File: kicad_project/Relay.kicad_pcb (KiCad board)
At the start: 2 copper layers, 36.6 x 28.3 mm, 13 parts, among them J1 5018762640, J2 USB_C_Receptacle, J3 RJ45, K1 G6K-2P-Y_DC5, Q1 CMPT5551

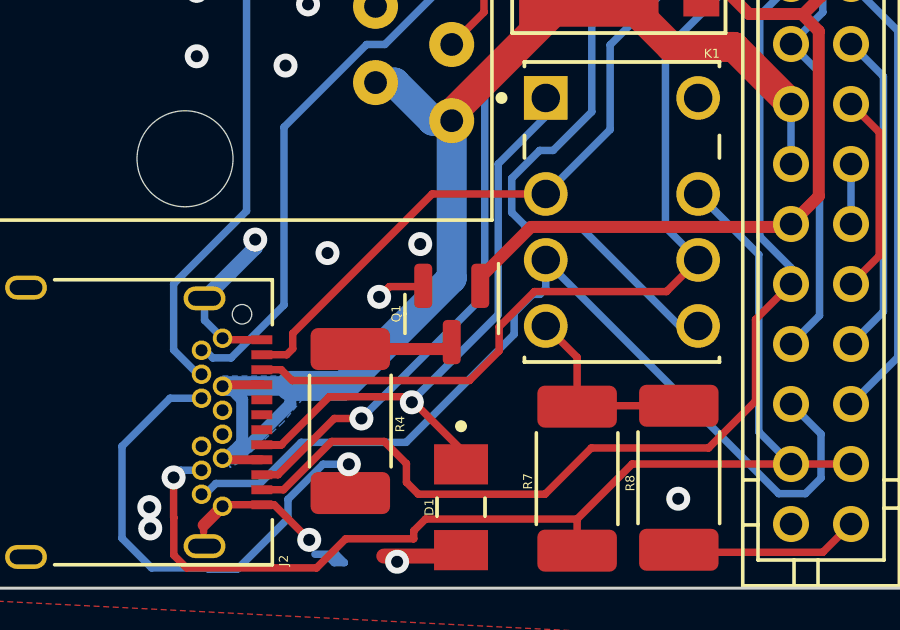
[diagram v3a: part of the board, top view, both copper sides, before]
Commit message: finally fixed Transistor Issue. credits to mlocoteta
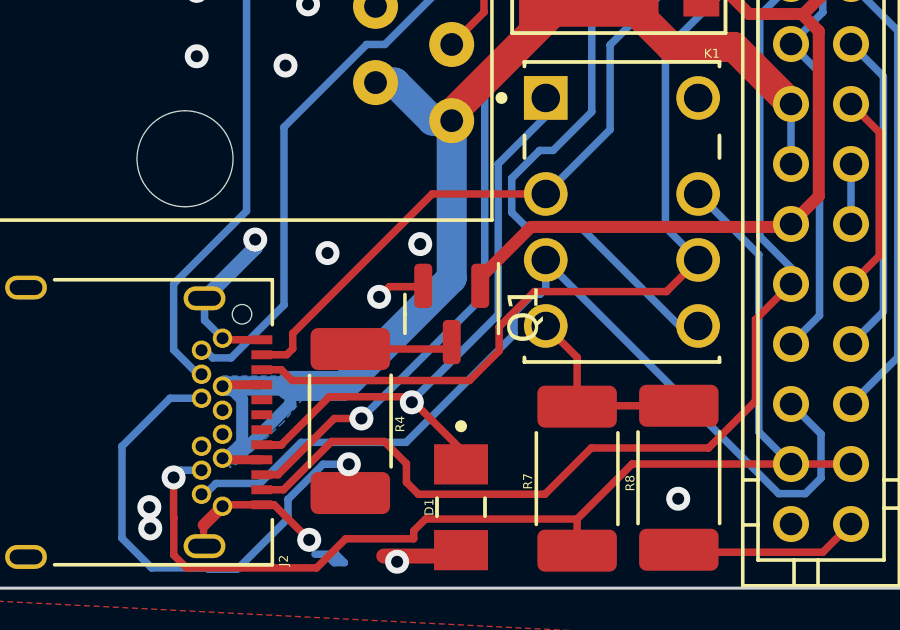
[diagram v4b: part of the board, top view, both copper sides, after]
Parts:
- Q1: value CMPT5551 -> DDTC114ECA-7-F
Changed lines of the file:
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@@
   (net 28 "CAN2_H")
   (net 29 "Relay_5")
-  (net 30 "Net-(Q1-Pad3)")
-  (footprint "Package_TO_SOT_SMD:SOT-23" (layer "F.Cu")
-    (at 162.84 71.59 -90)
-    (descr "SOT, 3 Pin (https://www.jedec.org/system/files/docs/to-236h.pdf variant AB), generated with kicad-footprint-generator ipc_gullwing_generator.py")
-    (tags "SOT TO_SOT_SMD")
-    (property "Sheetfile" "Relay.kicad_sch")
-    (property "Sheetname" "")
-    (attr smd)
-    (fp_text reference "Q1" (at -0.01 1.85 -90) (layer "F.SilkS")
-      (effects (font (size 0.3 0.3) (thickness 0.15)))
-    )
-    (fp_text value "CMPT5551" (at 0 2.4 90) (layer "F.Fab")
-      (effects (font (size 1 1) (thickness 0.15)))
-    )
-    (fp_text user "${REFERENCE}" (at 0 0 90) (layer "F.Fab")
-      (effects (font (size 0.32 0.32) (thickness 0.05)))
-    )
-    (fp_line (start 0 1.56) (end -0.65 1.56) (layer "F.SilkS") (width 0.12))
-    (fp_line (start 0 -1.56) (end -1.675 -1.56) (layer "F.SilkS") (width 0.12))
-    (fp_line (start 0 -1.56) (end 0.65 -1.56) (layer "F.SilkS") (width 0.12))
-    (fp_line (start 0 1.56) (end 0.65 1.56) (layer "F.SilkS") (width 0.12))
-    (fp_line (start 1.92 -1.7) (end -1.92 -1.7) (layer "F.CrtYd") (width 0.05))
-    (fp_line (start -1.92 -1.7) (end -1.92 1.7) (layer "F.CrtYd") (width 0.05))
-    (fp_line (start -1.92 1.7) (end 1.92 1.7) (layer "F.CrtYd") (width 0.05))
-    (fp_line (start 1.92 1.7) (end 1.92 -1.7) (layer "F.CrtYd") (width 0.05))
-    (fp_line (start -0.65 -1.125) (end -0.325 -1.45) (layer "F.Fab") (width 0.1))
-    (fp_line (start 0.65 -1.45) (end 0.65 1.45) (layer "F.Fab") (width 0.1))
-    (fp_line (start 0.65 1.45) (end -0.65 1.45) (layer "F.Fab") (width 0.1))
-    (fp_line (start -0.325 -1.45) (end 0.65 -1.45) (layer "F.Fab") (width 0.1))
-    (fp_line (start -0.65 1.45) (end -0.65 -1.125) (layer "F.Fab") (width 0.1))
-    (pad "1" smd roundrect (at -0.9375 -0.95 270) (size 1.475 0.6) (layers "F.Cu" "F.Paste" "F.Mask") (roundrect_rratio 0.25)
-      (net 3 "IGN") (pinfunction "B") (pintype "input"))
-    (pad "2" smd roundrect (at -0.9375 0.95 270) (size 1.475 0.6) (layers "F.Cu" "F.Paste" "F.Mask") (roundrect_rratio 0.25)
-      (net 2 "GND") (pinfunction "E") (pintype "passive"))
-    (pad "3" smd roundrect (at 0.9375 0 270) (size 1.475 0.6) (layers "F.Cu" "F.Paste" "F.Mask") (roundrect_rratio 0.25)
-      (net 30 "Net-(Q1-Pad3)") (pinfunction "C") (pintype "passive"))
-    (model "${KICAD6_3DMODEL_DIR}/Package_TO_SOT_SMD.3dshapes/SOT-23.wrl"
-      (offset (xyz 0 0 0))
-      (scale (xyz 1 1 1))
-      (rotate (xyz 0 0 0))
-    )
-  )
+  (net 30 "Net-(R4-Pad1)")
   (footprint "Relay:DIO_BAV21W_RHG" (layer "F.Cu")
     (at 163.15 78.0325 -90)
@@
     )
   )
+  (footprint "Package_TO_SOT_SMD:SOT-23" (layer "F.Cu")
+    (at 162.84 71.59 -90)
+    (descr "SOT, 3 Pin (https://www.jedec.org/system/files/docs/to-236h.pdf variant AB), generated with kicad-footprint-generator ipc_gullwing_generator.py")
+    (tags "SOT TO_SOT_SMD")
+    (property "Sheetfile" "Relay.kicad_sch")
+    (property "Sheetname" "")
+    (attr smd)
+    (fp_text reference "Q1" (at 0 -2.4 90) (layer "F.SilkS")
+      (effects (font (size 1 1) (thickness 0.15)))
+    )
+    (fp_text value "DDTC114ECA-7-F " (at 0 2.4 90) (layer "F.Fab")
+      (effects (font (size 1 1) (thickness 0.15)))
+    )
+    (fp_text user "${REFERENCE}" (at 0 0 90) (layer "F.Fab")
+      (effects (font (size 0.32 0.32) (thickness 0.05)))
+    )
+    (fp_line (start 0 1.56) (end 0.65 1.56) (layer "F.SilkS") (width 0.12))
+    (fp_line (start 0 -1.56) (end 0.65 -1.56) (layer "F.SilkS") (width 0.12))
+    (fp_line (start 0 1.56) (end -0.65 1.56) (layer "F.SilkS") (width 0.12))
+    (fp_line (start 0 -1.56) (end -1.675 -1.56) (layer "F.SilkS") (width 0.12))
+    (fp_line (start 1.92 1.7) (end 1.92 -1.7) (layer "F.CrtYd") (width 0.05))
+    (fp_line (start -1.92 -1.7) (end -1.92 1.7) (layer "F.CrtYd") (width 0.05))
+    (fp_line (start 1.92 -1.7) (end -1.92 -1.7) (layer "F.CrtYd") (width 0.05))
+    (fp_line (start -1.92 1.7) (end 1.92 1.7) (layer "F.CrtYd") (width 0.05))
+    (fp_line (start 0.65 -1.45) (end 0.65 1.45) (layer "F.Fab") (width 0.1))
+    (fp_line (start -0.65 -1.125) (end -0.325 -1.45) (layer "F.Fab") (width 0.1))
+    (fp_line (start -0.65 1.45) (end -0.65 -1.125) (layer "F.Fab") (width 0.1))
+    (fp_line (start 0.65 1.45) (end -0.65 1.45) (layer "F.Fab") (width 0.1))
+    (fp_line (start -0.325 -1.45) (end 0.65 -1.45) (layer "F.Fab") (width 0.1))
+    (pad "1" smd roundrect (at -0.9375 -0.95 270) (size 1.475 0.6) (layers "F.Cu" "F.Paste" "F.Mask") (roundrect_rratio 0.25)
+      (net 3 "IGN") (pinfunction "B") (pintype "input"))
+    (pad "2" smd roundrect (at -0.9375 0.95 270) (size 1.475 0.6) (layers "F.Cu" "F.Paste" "F.Mask") (roundrect_rratio 0.25)
+      (net 2 "GND") (pinfunction "E") (pintype "passive"))
+    (pad "3" smd roundrect (at 0.9375 0 270) (size 1.475 0.6) (layers "F.Cu" "F.Paste" "F.Mask") (roundrect_rratio 0.25)
+      (net 30 "Net-(R4-Pad1)") (pinfunction "C") (pintype "passive"))
+    (model "${KICAD6_3DMODEL_DIR}/Package_TO_SOT_SMD.3dshapes/SOT-23.wrl"
+      (offset (xyz 0 0 0))
+      (scale (xyz 1 1 1))
+      (rotate (xyz 0 0 0))
+    )
+  )
   (footprint "Resistor_SMD:R_0603_1608Metric" (layer "F.Cu")
     (at 166.15 56.71 180)
@@
     (fp_line (start -2.5 1.25) (end -2.5 -1.25) (layer "F.Fab") (width 0.1))
     (pad "1" smd roundrect (at -2.4 0 270) (size 1.4 2.65) (layers "F.Cu" "F.Paste" "F.Mask") (roundrect_rratio 0.1785707143)
-      (net 30 "Net-(Q1-Pad3)") (pintype "passive"))
+      (net 30 "Net-(R4-Pad1)") (pintype "passive"))
     (pad "2" smd roundrect (at 2.4 0 270) (size 1.4 2.65) (layers "F.Cu" "F.Paste" "F.Mask") (roundrect_rratio 0.1785707143)
       (net 21 "SBU2") (pintype "passive"))
@@
   (segment (start 167.5086 64.8514) (end 166.22 66.14) (width 0.25) (layer "B.Cu") (net 29))
   (segment (start 170.43 71.99) (end 171.0545 71.99) (width 0.25) (layer "B.Cu") (net 29))
-  (segment (start 159.46 72.76) (end 162.6075 72.76) (width 0.4) (layer "F.Cu") (net 30))
   (segment (start 162.6075 72.76) (end 162.84 72.5275) (width 0.25) (layer "F.Cu") (net 30))
+  (segment (start 159.46 72.76) (end 162.6075 72.76) (width 0.25) (layer "F.Cu") (net 30))
   (zone (net 2) (net_name "GND") (layer "F.Cu") (hatch edge 0.508)
     (connect_pads (clearance 0.508))

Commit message: tested
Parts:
- moved R5 5.46 mm to (170.6, 53.5)
- moved D1 4.78 mm to (160.1, 74.4), turned to 90 degrees
- moved R6 3.92 mm to (166.8, 53.5)
- moved R4 3.87 mm to (163.0, 76.7)
- moved R1 1.84 mm to (168.7, 55.9)
- moved Q1 0.68 mm to (163.1, 71.0)
- turned CR1 to 180 degrees
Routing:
- net GND: track 16.5 -> 59.1 mm, vias 18 -> 12
- net CAN1_L: track 54.3 -> 30.7 mm, vias 1 -> 0
- net CAN0_L: track 38.2 -> 50.0 mm, vias 0 -> 3
- net CAN0_H: track 32.4 -> 41.8 mm, vias 0 -> 2
- net Net-(J3-Pad3): track 6.29 -> 13.2 mm
- net +12V: track 45.3 -> 39.6 mm
- net Relay_5: track 25.8 -> 20.1 mm
- net CAN3_H: track 17.5 -> 22.0 mm
- net Net-(J1-Pad5): track 13.5 -> 17.6 mm
- net CAN2_L: track 39.5 -> 42.7 mm
- net CAN3_L: track 22.4 -> 25.2 mm
- net IGN: track 37.5 -> 39.4 mm, vias 0 -> 2
- net CAN2_H: track 31.2 -> 32.5 mm
- net Net-(J1-Pad21): track 15.3 -> 16.5 mm
- net SBU1: track 21.2 -> 20.0 mm, vias 1 -> 0
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- added copper zone on F.Cu, net +12V
- removed copper zone on B.Cu, net +12V
- removed copper zone on F.Cu, net GND
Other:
- board text added: "-"

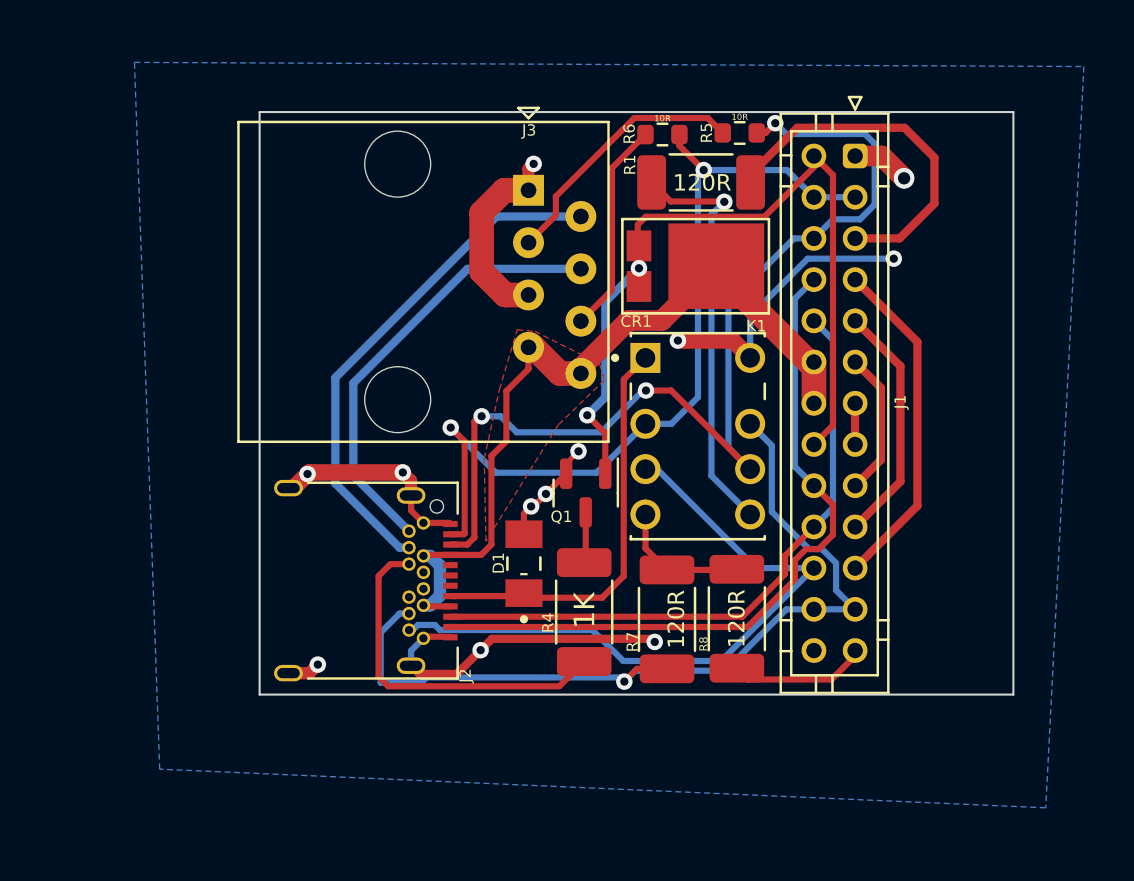
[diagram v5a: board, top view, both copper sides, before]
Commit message: update usb-c and pcb
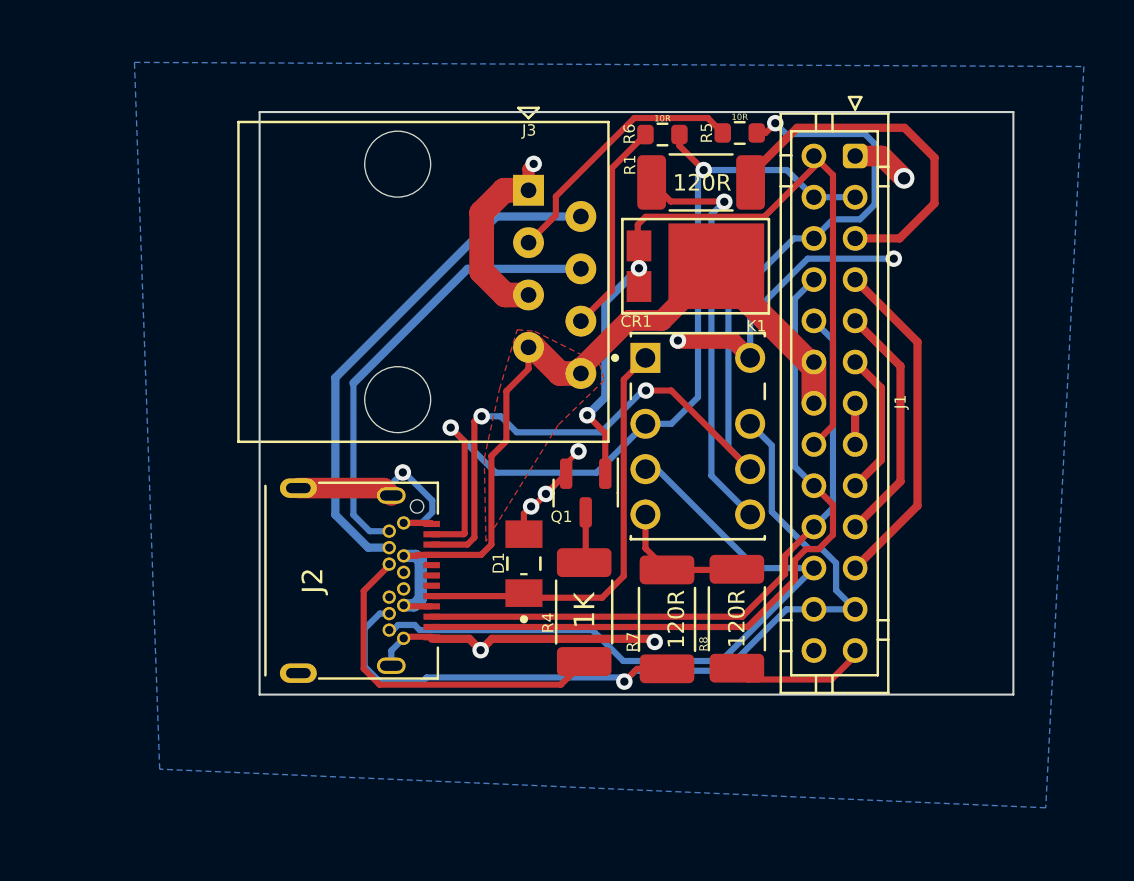
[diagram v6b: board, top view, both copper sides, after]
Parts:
- J2: footprint Connector_USB:USB_C_Receptacle_Amphenol_12401548E4-2A -> Relay:TYPE-C-31-M-04
- moved J2 0.96 mm to (150.5, 75.2)
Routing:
- net GND: track 59.1 -> 57.6 mm, vias 12 -> 10
- net +12V: track 39.6 -> 40.8 mm
- net CAN2_H: track 32.5 -> 33.5 mm
- net SBU1: track 20.0 -> 20.9 mm
- net CAN1_H: track 34.5 -> 35.4 mm
- net CAN0_L: track 50.0 -> 50.9 mm
- net CAN0_H: track 41.8 -> 42.7 mm
- net CAN1_L: track 30.7 -> 31.6 mm
